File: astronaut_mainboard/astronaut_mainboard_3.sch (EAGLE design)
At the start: 23 parts, among them IC1 ADUM1250, IC2 741G3157DBVR, IC3 741G3157DBVR, J10 HF Comm, J6 Ext 5V, J7 UI, J8 Arduino (DWM), J9 GNSS, Q1 BSS138, Q3 BSS138

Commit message: updated lib, corrected boards (after printing)
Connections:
- net +5V: no longer J6-2.S
- net GND: now also J6-2.S
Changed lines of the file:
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@@
 <pinref part="SUPPLY13" gate="GND" pin="GND"/>
 <pinref part="J6" gate="-1" pin="S"/>
-<wire x1="38.1" y1="88.9" x2="53.34" y2="88.9" width="0.1524" layer="91"/>
+<wire x1="38.1" y1="88.9" x2="48.26" y2="88.9" width="0.1524" layer="91"/>
+<pinref part="J6" gate="-2" pin="S"/>
+<wire x1="48.26" y1="88.9" x2="53.34" y2="88.9" width="0.1524" layer="91"/>
+<wire x1="53.34" y1="86.36" x2="48.26" y2="86.36" width="0.1524" layer="91"/>
+<wire x1="48.26" y1="86.36" x2="48.26" y2="88.9" width="0.1524" layer="91"/>
+<junction x="48.26" y="88.9"/>
 </segment>
 </net>
@@
 <wire x1="38.1" y1="86.36" x2="40.64" y2="86.36" width="0.1524" layer="91"/>
 <pinref part="SUPPLY14" gate="+5V" pin="+5V"/>
-<pinref part="J6" gate="-2" pin="S"/>
-<wire x1="40.64" y1="86.36" x2="53.34" y2="86.36" width="0.1524" layer="91"/>
-<junction x="40.64" y="86.36"/>
 <wire x1="40.64" y1="86.36" x2="40.64" y2="83.82" width="0.1524" layer="91"/>
 <pinref part="J6" gate="-3" pin="S"/>

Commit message: verified, ready to production
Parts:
- LED1: device led:LED3MM -> led:LEDSML1206
- R17: value 470 -> 100
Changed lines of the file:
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@@
 <grid distance="0.1" unitdist="inch" unit="inch" style="lines" multiple="1" display="no" altdistance="0.01" altunitdist="inch" altunit="inch"/>
 <layers>
-<layer number="1" name="Top" color="4" fill="1" visible="no" active="no"/>
-<layer number="16" name="Bottom" color="1" fill="1" visible="no" active="no"/>
-<layer number="17" name="Pads" color="2" fill="1" visible="no" active="no"/>
-<layer number="18" name="Vias" color="2" fill="1" visible="no" active="no"/>
-<layer number="19" name="Unrouted" color="6" fill="1" visible="no" active="no"/>
-<layer number="20" name="Dimension" color="15" fill="1" visible="no" active="no"/>
-<layer number="21" name="tPlace" color="7" fill="1" visible="no" active="no"/>
-<layer number="22" name="bPlace" color="7" fill="1" visible="no" active="no"/>
-<layer number="23" name="tOrigins" color="15" fill="1" visible="no" active="no"/>
-<layer number="24" name="bOrigins" color="15" fill="1" visible="no" active="no"/>
-<layer number="25" name="tNames" color="7" fill="1" visible="no" active="no"/>
-<layer number="26" name="bNames" color="7" fill="1" visible="no" active="no"/>
-<layer number="27" name="tValues" color="7" fill="1" visible="no" active="no"/>
-<layer number="28" name="bValues" color="7" fill="1" visible="no" active="no"/>
+<layer number="1" name="Top" color="4" fill="1" visible="yes" active="no"/>
+<layer number="16" name="Bottom" color="1" fill="1" visible="yes" active="no"/>
+<layer number="17" name="Pads" color="2" fill="1" visible="yes" active="no"/>
+<layer number="18" name="Vias" color="2" fill="1" visible="yes" active="no"/>
+<layer number="19" name="Unrouted" color="6" fill="1" visible="yes" active="no"/>
+<layer number="20" name="Dimension" color="15" fill="1" visible="yes" active="no"/>
+<layer number="21" name="tPlace" color="7" fill="1" visible="yes" active="no"/>
+<layer number="22" name="bPlace" color="7" fill="1" visible="yes" active="no"/>
+<layer number="23" name="tOrigins" color="15" fill="1" visible="yes" active="no"/>
+<layer number="24" name="bOrigins" color="15" fill="1" visible="yes" active="no"/>
+<layer number="25" name="tNames" color="7" fill="1" visible="yes" active="no"/>
+<layer number="26" name="bNames" color="7" fill="1" visible="yes" active="no"/>
+<layer number="27" name="tValues" color="7" fill="1" visible="yes" active="no"/>
+<layer number="28" name="bValues" color="7" fill="1" visible="yes" active="no"/>
 <layer number="29" name="tStop" color="7" fill="3" visible="no" active="no"/>
 <layer number="30" name="bStop" color="7" fill="6" visible="no" active="no"/>
@@
 <layer number="35" name="tGlue" color="7" fill="4" visible="no" active="no"/>
 <layer number="36" name="bGlue" color="7" fill="5" visible="no" active="no"/>
-<layer number="37" name="tTest" color="7" fill="1" visible="no" active="no"/>
-<layer number="38" name="bTest" color="7" fill="1" visible="no" active="no"/>
+<layer number="37" name="tTest" color="7" fill="1" visible="yes" active="no"/>
+<layer number="38" name="bTest" color="7" fill="1" visible="yes" active="no"/>
 <layer number="39" name="tKeepout" color="4" fill="11" visible="no" active="no"/>
 <layer number="40" name="bKeepout" color="1" fill="11" visible="no" active="no"/>
@@
 <layer number="44" name="Drills" color="7" fill="1" visible="no" active="no"/>
 <layer number="45" name="Holes" color="7" fill="1" visible="no" active="no"/>
-<layer number="46" name="Milling" color="3" fill="1" visible="no" active="no"/>
-<layer number="47" name="Measures" color="7" fill="1" visible="no" active="no"/>
-<layer number="48" name="Document" color="7" fill="1" visible="no" active="no"/>
-<layer number="49" name="Reference" color="7" fill="1" visible="no" active="no"/>
-<layer number="50" name="dxf" color="7" fill="1" visible="no" active="no"/>
-<layer number="51" name="tDocu" color="7" fill="1" visible="no" active="no"/>
-<layer number="52" name="bDocu" color="7" fill="1" visible="no" active="no"/>
-<layer number="53" name="tPadExt" color="7" fill="1" visible="no" active="no"/>
-<layer number="54" name="bPadExt" color="1" fill="1" visible="no" active="no"/>
-<layer number="56" name="wert" color="7" fill="1" visible="no" active="no"/>
-<layer number="57" name="tCAD" color="7" fill="1" visible="no" active="no"/>
-<layer number="59" name="tCarbon" color="7" fill="1" visible="no" active="no"/>
-<layer number="60" name="bCarbon" color="7" fill="1" visible="no" active="no"/>
+<layer number="46" name="Milling" color="3" fill="1" visible="yes" active="no"/>
+<layer number="47" name="Measures" color="7" fill="1" visible="yes" active="no"/>
+<layer number="48" name="Document" color="7" fill="1" visible="yes" active="no"/>
+<layer number="49" name="Reference" color="7" fill="1" visible="yes" active="no"/>
+<layer number="50" name="dxf" color="7" fill="1" visible="yes" active="no"/>
+<layer number="51" name="tDocu" color="7" fill="1" visible="yes" active="no"/>
+<layer number="52" name="bDocu" color="7" fill="1" visible="yes" active="no"/>
+<layer number="53" name="tPadExt" color="7" fill="1" visible="yes" active="no"/>
+<layer number="54" name="bPadExt" color="1" fill="1" visible="yes" active="no"/>
+<layer number="56" name="wert" color="7" fill="1" visible="yes" active="no"/>
+<layer number="57" name="tCAD" color="7" fill="1" visible="yes" active="no"/>
+<layer number="59" name="tCarbon" color="7" fill="1" visible="yes" active="no"/>
+<layer number="60" name="bCarbon" color="7" fill="1" visible="yes" active="no"/>
 <layer number="88" name="SimResults" color="9" fill="1" visible="yes" active="yes"/>
 <layer number="89" name="SimProbes" color="9" fill="1" visible="yes" active="yes"/>
@@
 <part name="SUPPLY29" library="supply2" deviceset="VCC" device=""/>
 <part name="SUPPLY30" library="supply2" deviceset="GND" device=""/>
-<part name="LED1" library="led" deviceset="LED" device="3MM"/>
-<part name="R17" library="rcl" deviceset="R-EU_" device="R0805" value="470"/>
+<part name="LED1" library="led" deviceset="LED" device="SML1206"/>
+<part name="R17" library="rcl" deviceset="R-EU_" device="R0805" value="100"/>
 <part name="SUPPLY31" library="supply2" deviceset="GND" device=""/>
 <part name="R1" library="rcl" deviceset="R-EU_" device="R0805" value="10k"/>

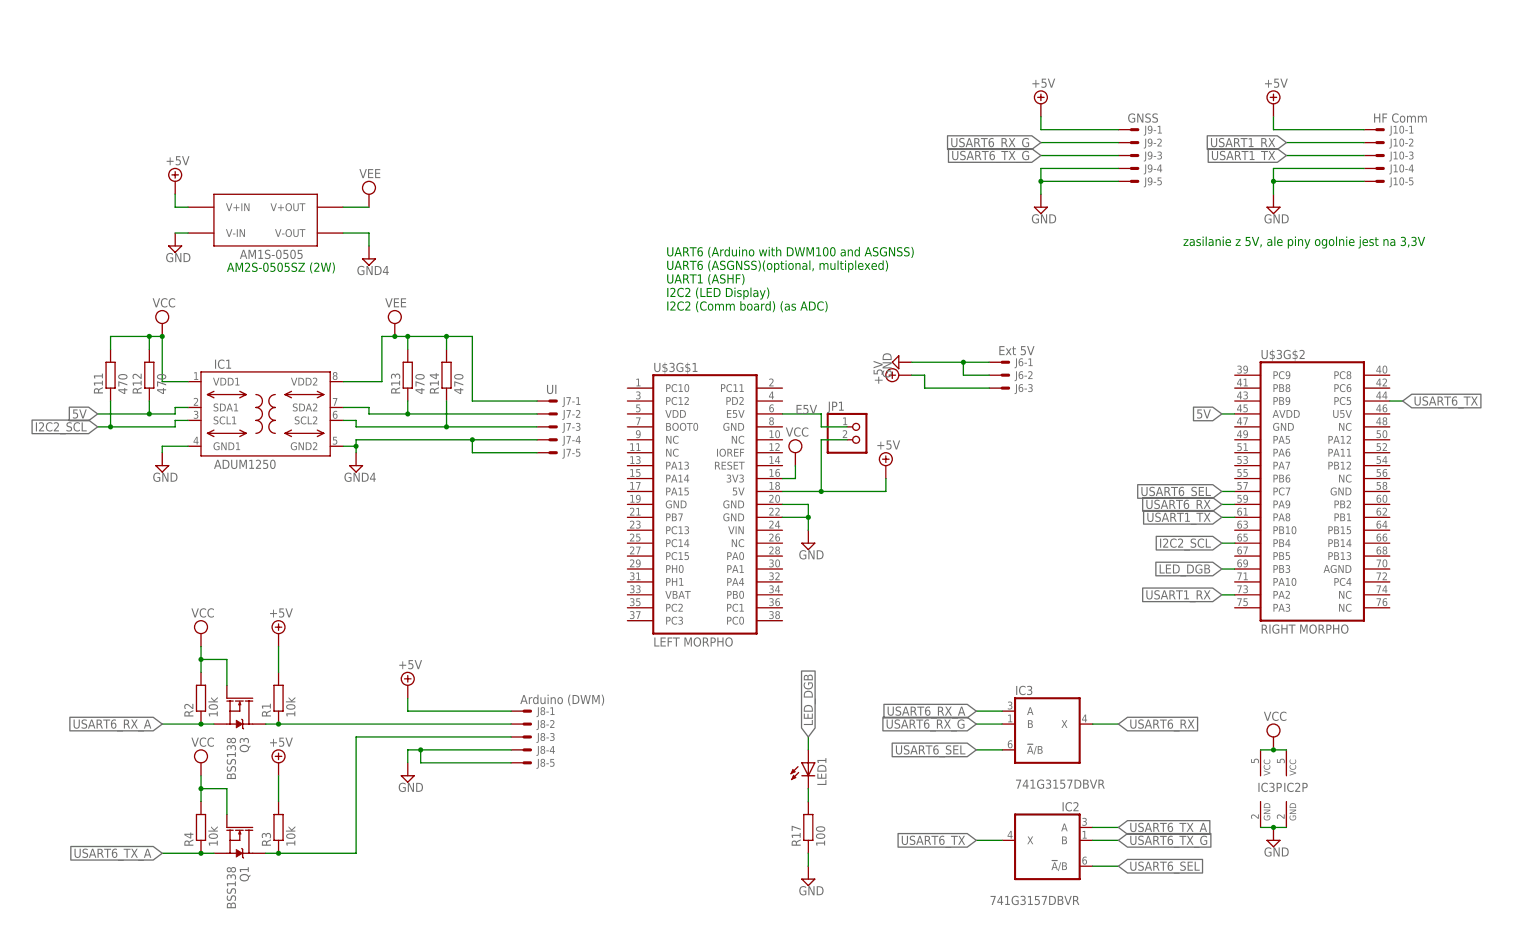
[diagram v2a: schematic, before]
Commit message: corrected gerbers, cleaned schematics, added documnetation
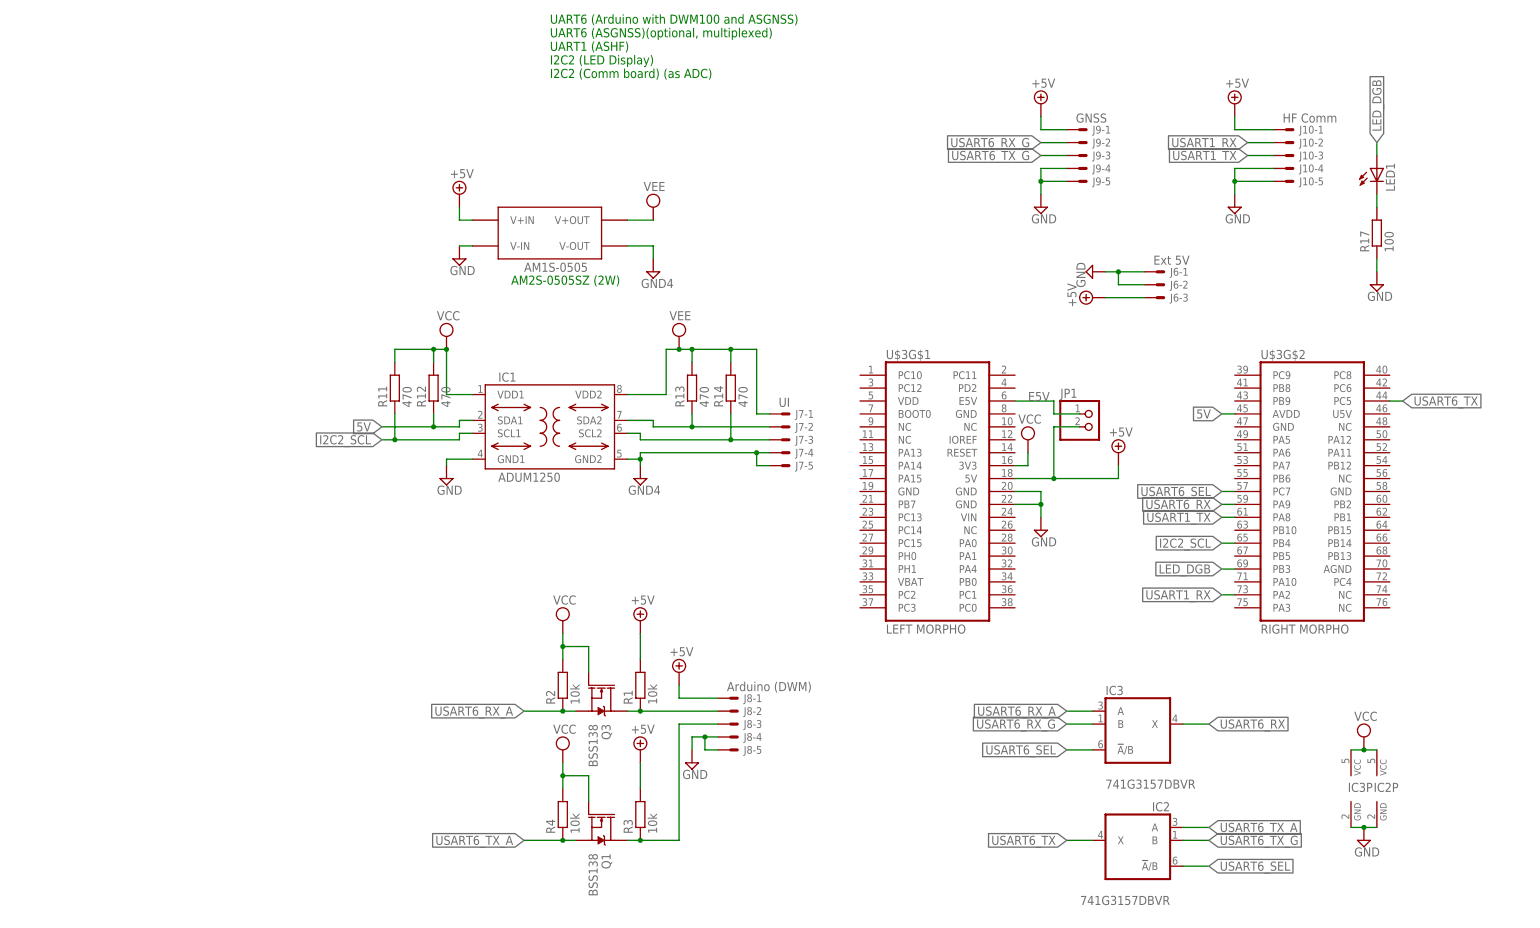
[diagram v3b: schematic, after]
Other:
- note added: "Arduino DWM (IO)"
- note added: "Other connectors"
- note added: "UART Switch"
- note added: "User Interface (IO)"
- note removed: "zasilanie z 5V, ale piny ogolnie jest na 3,3V"
- moved on the sheet: IC1, IC2, IC2P, IC3, IC3P, J10-1, J10-2, J10-3, J10-4, J10-5, J6-1, J6-2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
